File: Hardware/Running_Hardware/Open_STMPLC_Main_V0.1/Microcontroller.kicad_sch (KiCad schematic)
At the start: 73 parts, among them J1 Conn_02x08_Odd_Even, J12 USB C, J2 USB C, J3 Conn_01x04, SW1 Switch_6x6, U1 STM32F407IGTx, U3 TPS3430WDRC, U4 CH340C, Y1 48MHz, Y2 32.768kHz

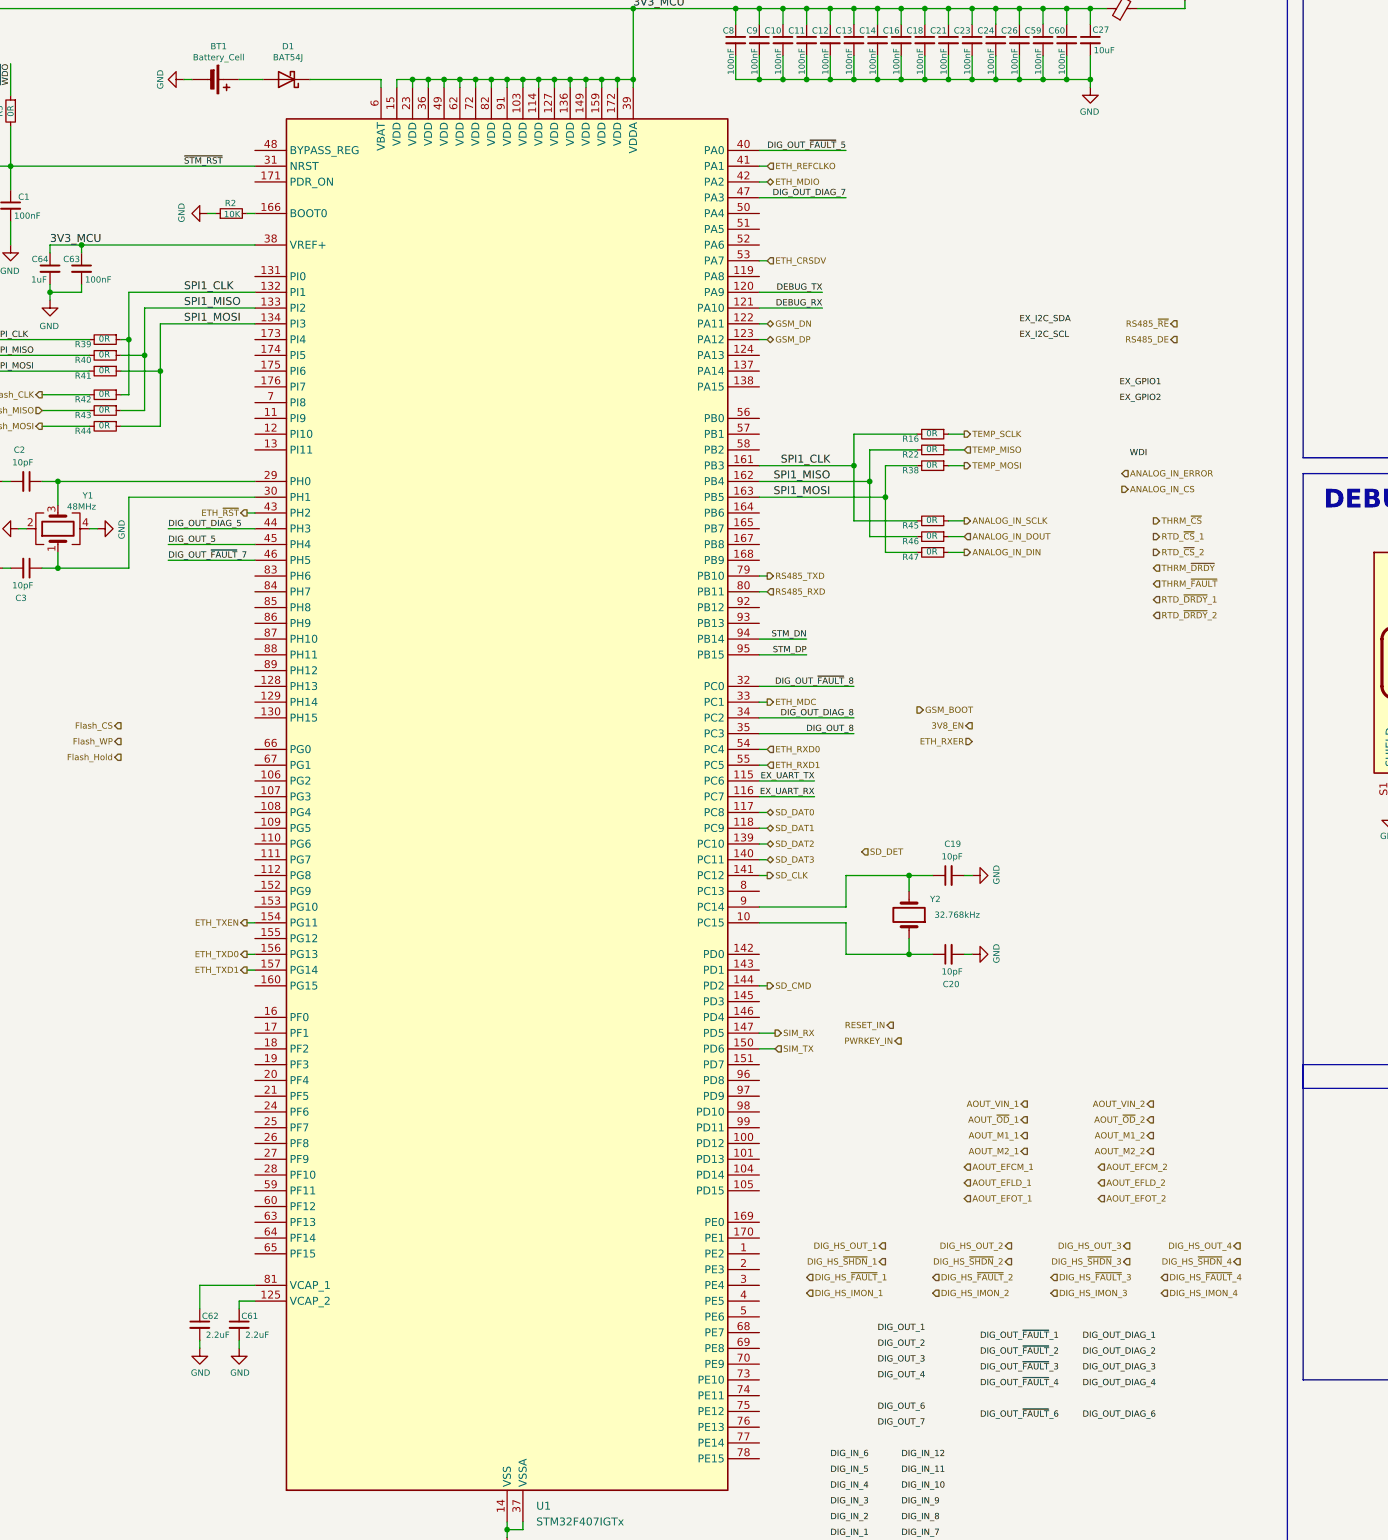
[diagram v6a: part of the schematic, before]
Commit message: Pin mapping - MCU connectors
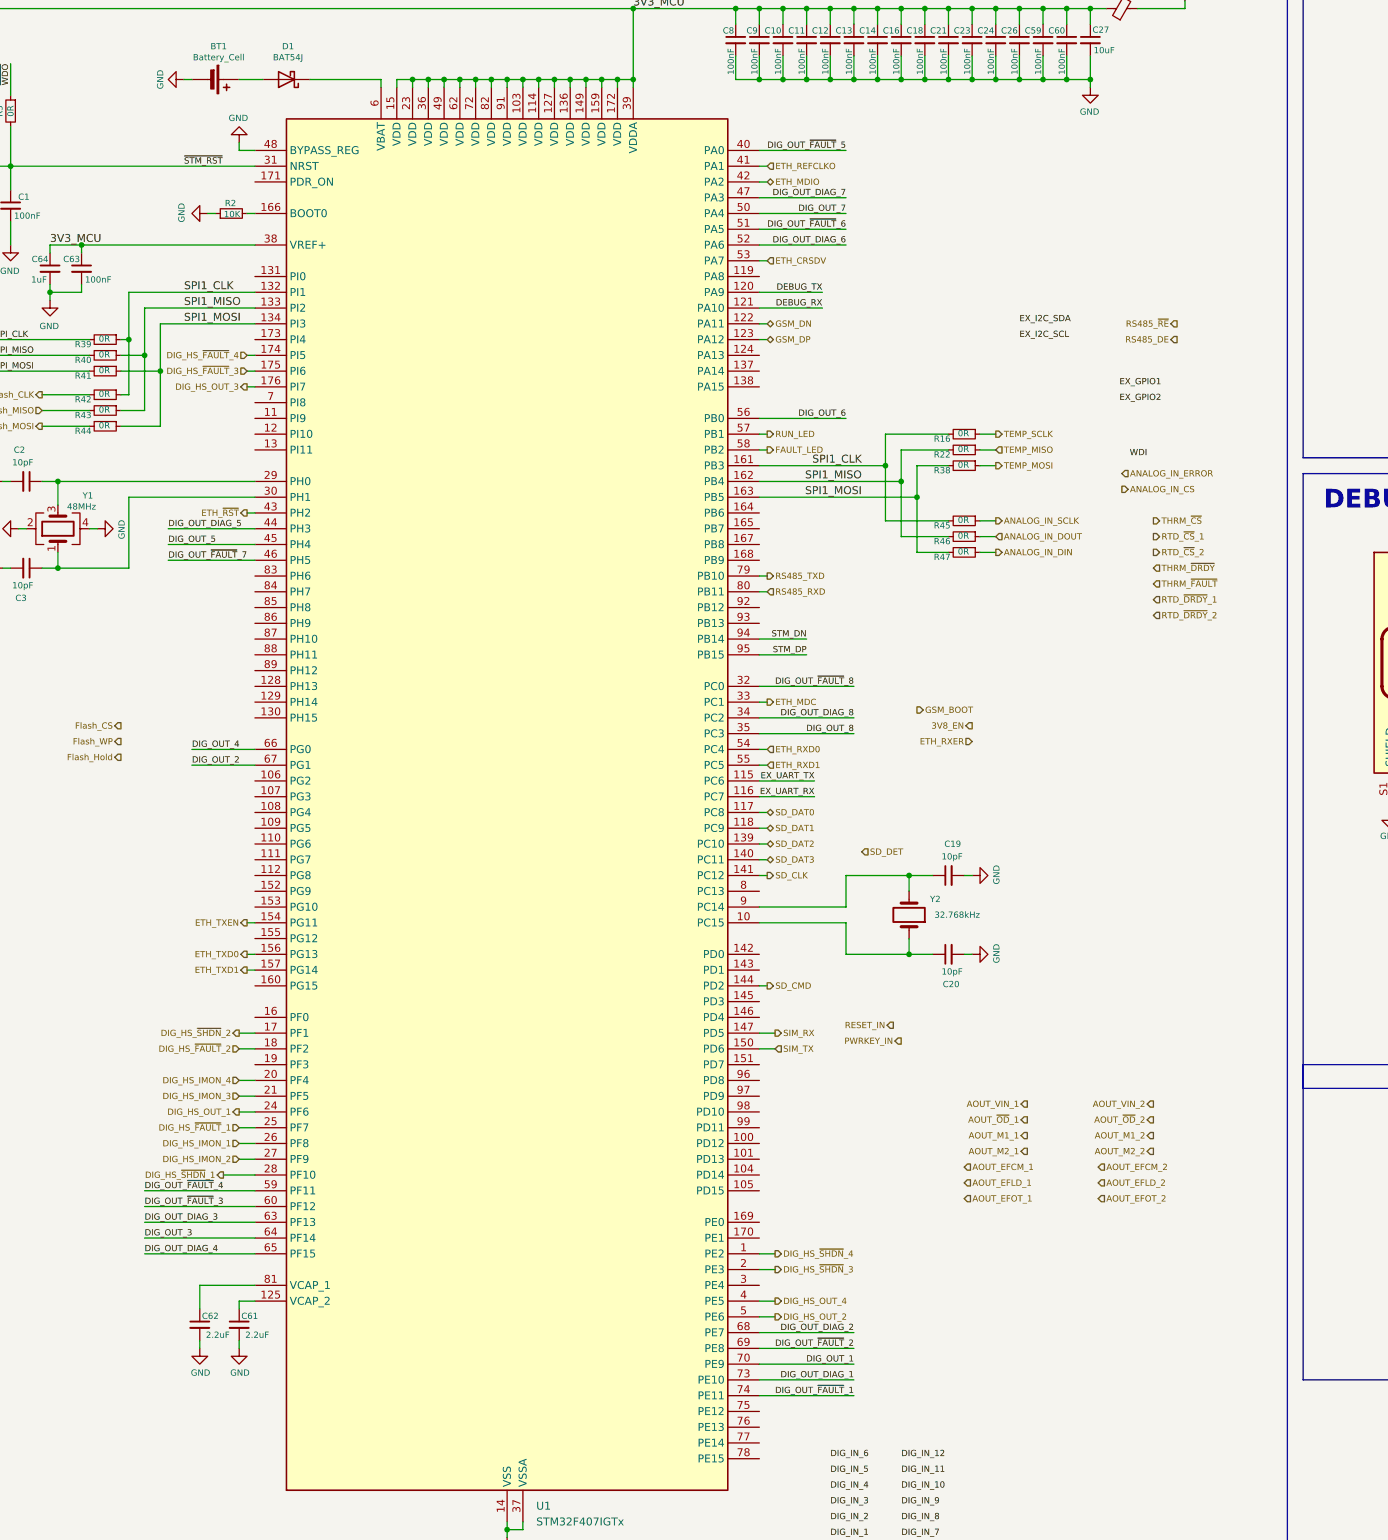
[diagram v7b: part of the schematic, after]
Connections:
- net DIG_HS_IMON_1: now also U1.26 (PF8)
- net DIG_HS_IMON_2: now also U1.27 (PF9)
- net DIG_HS_IMON_3: now also U1.21 (PF5)
- net DIG_HS_IMON_4: now also U1.20 (PF4)
- net DIG_HS_OUT_1: now also U1.24 (PF6)
- net DIG_HS_OUT_2: now also U1.5 (PE6)
- net DIG_HS_OUT_3: now also U1.176 (PI7)
- net DIG_HS_OUT_4: now also U1.4 (PE5)
- net DIG_HS_~{FAULT}_1: now also U1.25 (PF7)
- net DIG_HS_~{FAULT}_2: now also U1.18 (PF2)
- net DIG_HS_~{FAULT}_3: now also U1.175 (PI6)
- net DIG_HS_~{FAULT}_4: now also U1.174 (PI5)
- net DIG_HS_~{SHDN}_1: now also U1.28 (PF10)
- net DIG_HS_~{SHDN}_2: now also U1.17 (PF1)
- net DIG_HS_~{SHDN}_3: now also U1.2 (PE3)
- net DIG_HS_~{SHDN}_4: now also U1.1 (PE2)
- net DIG_OUT_1: now also U1.70 (PE9)
- net DIG_OUT_2: now also U1.67 (PG1)
- net DIG_OUT_3: now also U1.64 (PF14)
- net DIG_OUT_4: now also U1.66 (PG0)
- net DIG_OUT_6: now also U1.56 (PB0)
- net DIG_OUT_7: now also U1.50 (PA4)
- net DIG_OUT_DIAG_1: now also U1.73 (PE10)
- net DIG_OUT_DIAG_2: now also U1.68 (PE7)
- net DIG_OUT_DIAG_3: now also U1.63 (PF13)
- net DIG_OUT_DIAG_4: now also U1.65 (PF15)
- net DIG_OUT_DIAG_6: now also U1.52 (PA6)
- net DIG_OUT_~{FAULT}_1: now also U1.74 (PE11)
- net DIG_OUT_~{FAULT}_2: now also U1.69 (PE8)
- net DIG_OUT_~{FAULT}_3: now also U1.60 (PF12)
- net DIG_OUT_~{FAULT}_4: now also U1.59 (PF11)
- net DIG_OUT_~{FAULT}_6: now also U1.51 (PA5)
- net GND: now also U1.48 (BYPASS_REG)
- net RUN_LED: now reaches U1.57 (PB1)
- net FAULT_LED: now reaches U1.58 (PB2)
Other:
- moved on the sheet: R16, R22, R38, R45, R46, R47
